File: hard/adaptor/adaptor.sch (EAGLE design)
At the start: 2 parts

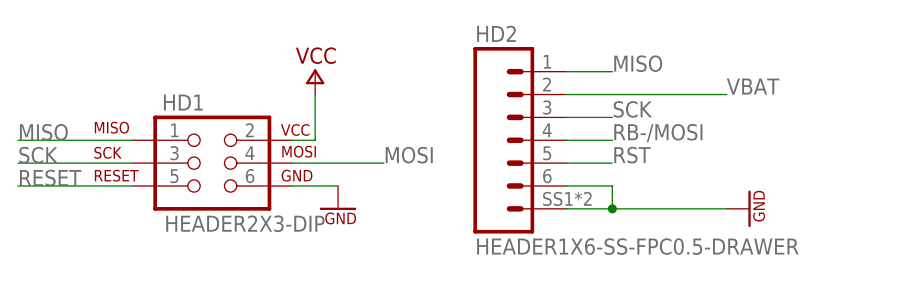
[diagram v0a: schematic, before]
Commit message: Add ISP adaptor board
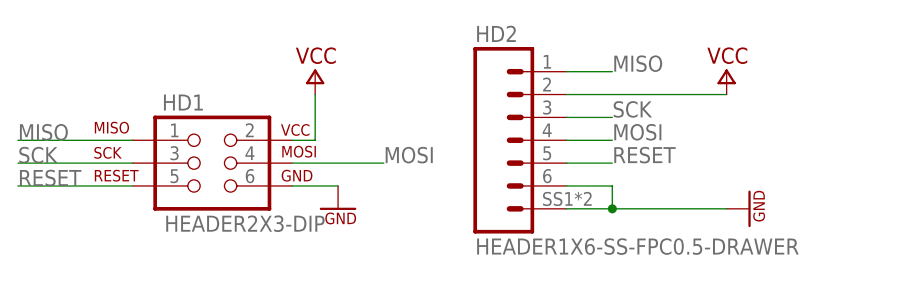
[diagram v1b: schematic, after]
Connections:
- removed net RB-/MOSI: HD2.4
- removed net RST: HD2.5
- removed net VBAT: HD2.2
- net MOSI: now also HD2.4
- net RESET: now also HD2.5
- net VCC: now also HD2.2
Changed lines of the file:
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@@
 <setting verticaltext="up"/>
 </settings>
-<grid distance="0.1" unitdist="inch" unit="inch" style="lines" multiple="1" display="yes" altdistance="0.01" altunitdist="inch" altunit="inch"/>
+<grid distance="0.1" unitdist="inch" unit="inch" style="lines" multiple="1" display="no" altdistance="0.01" altunitdist="inch" altunit="inch"/>
 <layers>
 <layer number="1" name="Top" color="4" fill="1" visible="no" active="no"/>
@@
 <part name="SUPPLY25" library="MyLibrary" deviceset="GND" device=""/>
 <part name="HD2" library="MyLibrary" deviceset="HEADER1X6-SS" device="-FPC0.5-DRAWER"/>
+<part name="SUPPLY3" library="MyLibrary" deviceset="VCC" device=""/>
 </parts>
 <sheets>
@@
 <instance part="SUPPLY25" gate="GND" x="40.64" y="-5.08" rot="R90"/>
 <instance part="HD2" gate="A" x="15.24" y="2.54"/>
+<instance part="SUPPLY3" gate="VCC" x="38.1" y="10.16"/>
 </instances>
 <busses>
@@
 <pinref part="HD1" gate="A" pin="2"/>
 <wire x1="-7.62" y1="2.54" x2="-10.16" y2="2.54" width="0.1524" layer="91"/>
+</segment>
+<segment>
+<wire x1="20.32" y1="7.62" x2="38.1" y2="7.62" width="0.1524" layer="91"/>
+<pinref part="HD2" gate="A" pin="2"/>
+<pinref part="SUPPLY3" gate="VCC" pin="VCC"/>
 </segment>
 </net>
@@
 <label x="0" y="0" size="1.778" layer="95" font="vector"/>
 </segment>
+<segment>
+<wire x1="20.32" y1="2.54" x2="25.4" y2="2.54" width="0.1524" layer="91"/>
+<label x="25.4" y="2.54" size="1.778" layer="95" font="vector"/>
+<pinref part="HD2" gate="A" pin="4"/>
+</segment>
 </net>
 <net name="MISO" class="0">
@@
 <label x="-40.64" y="-2.54" size="1.778" layer="95" font="vector"/>
 </segment>
-</net>
-<net name="RB-/MOSI" class="0">
-<segment>
-<wire x1="20.32" y1="2.54" x2="25.4" y2="2.54" width="0.1524" layer="91"/>
-<label x="25.4" y="2.54" size="1.778" layer="95" font="vector"/>
-<pinref part="HD2" gate="A" pin="4"/>
-</segment>
-</net>
-<net name="VBAT" class="0">
-<segment>
-<wire x1="20.32" y1="7.62" x2="38.1" y2="7.62" width="0.1524" layer="91"/>
-<pinref part="HD2" gate="A" pin="2"/>
-<label x="38.1" y="7.62" size="1.778" layer="95" font="vector"/>
-</segment>
-</net>
-<net name="RST" class="0">
 <segment>
 <pinref part="HD2" gate="A" pin="5"/>
